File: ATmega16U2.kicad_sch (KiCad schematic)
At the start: 28 parts, among them J1 Conn_02x02_Odd_Even, J12 USB_B, J2 Conn_02x03_Top_Bottom, J3 Conn_PIC_ICSP_ICD, U3 ATmega16U2-A, Y2 Crystal

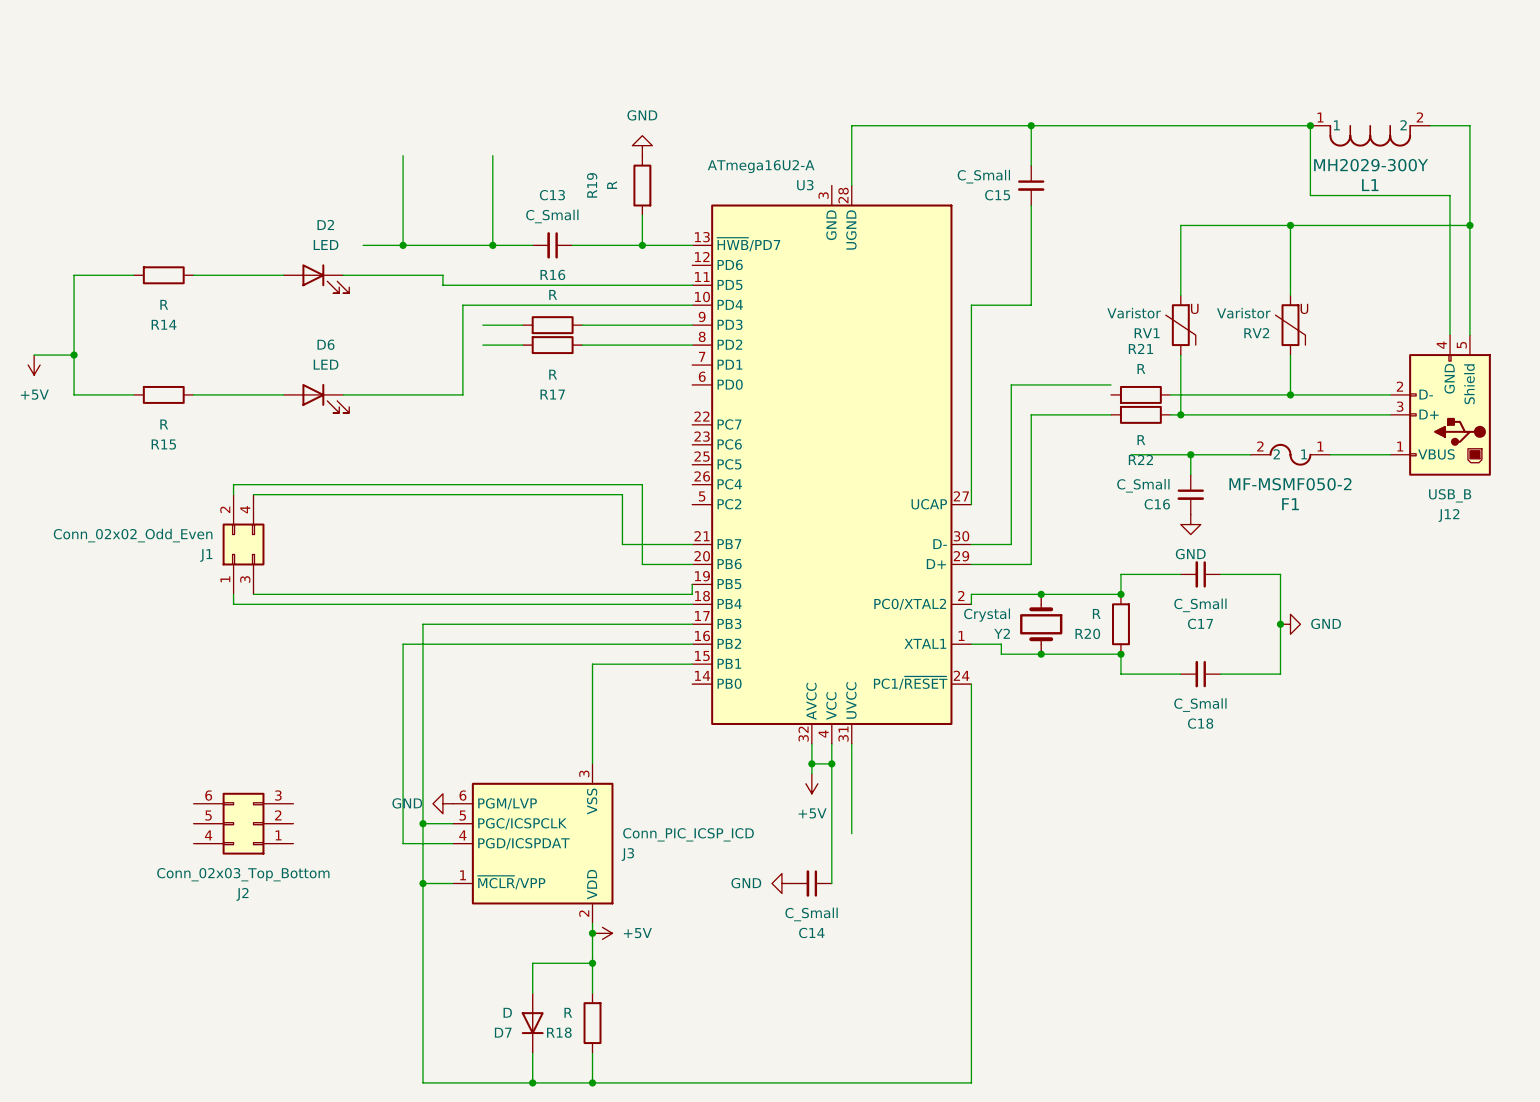
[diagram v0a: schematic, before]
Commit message: finished the schematic without mpower supply
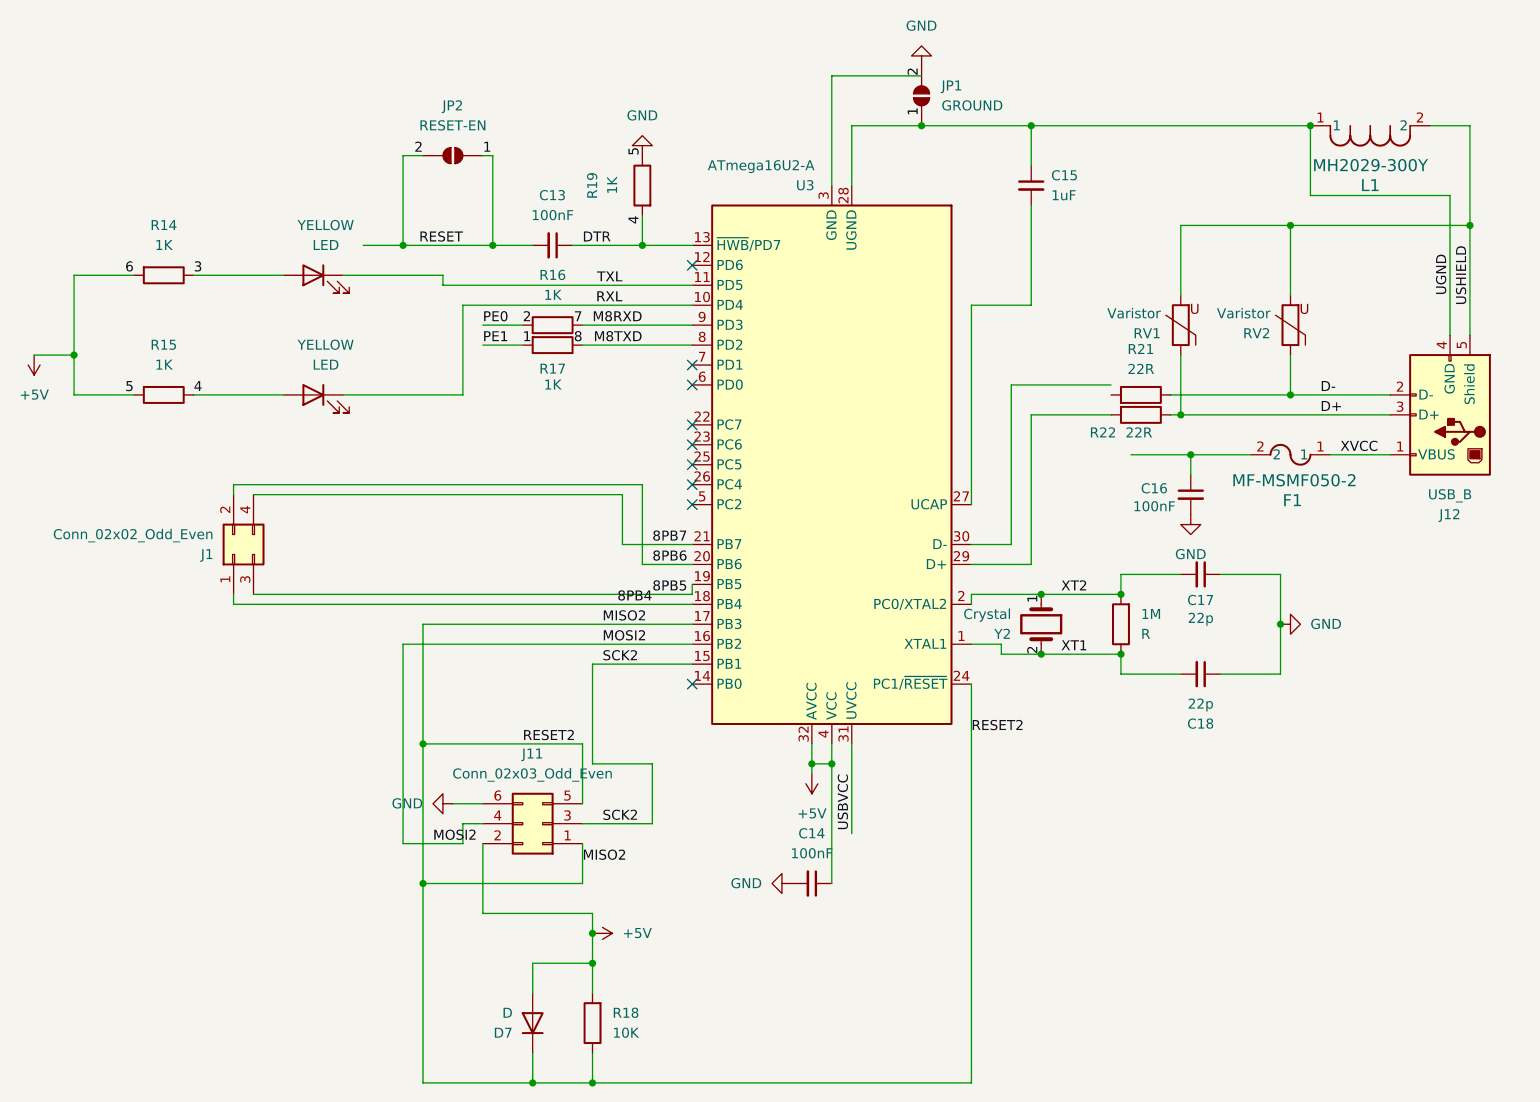
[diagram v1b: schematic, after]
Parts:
- removed J2: Conn_02x03_Top_Bottom, symbol Connector_Generic:Conn_02x03_Top_Bottom
- removed J3: Conn_PIC_ICSP_ICD, symbol Connector:Conn_PIC_ICSP_ICD
- added J11: Conn_02x03_Odd_Even, symbol Connector_Generic:Conn_02x03_Odd_Even
- added JP1: GROUND, symbol Jumper:SolderJumper_2_Open
- added JP2: RESET-EN, symbol Jumper:SolderJumper_2_Open
- C13, C14, C16: value C_Small -> 100nF
- C15: value C_Small -> 1uF
- C17, C18: value C_Small -> 22p
- R14, R15, R16, R17, R19: value R -> 1K
- R18: value R -> 10K
- R21, R22: value R -> 22R
- renumbered R20 to 1M, D2 to YELLOW, D6 to YELLOW
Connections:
- net GND is gone; now on net +5V: C14.2, C16.2, C17.1, C18.1, R19.1
- net +5V: now also J11.2 (Pin_2), J11.6 (Pin_6), JP1.2 (B)
- net D-: now reaches J12.2 (D-), R21.1, RV2.1
- net USHIELD: now reaches J12.5 (Shield), L1.2, RV1.2, RV2.2
- net 4: now reaches R15.1, YELLOW.2 (A)
- net 4: now also C13.1, R19.2, U3.13 (~{HWB}/PD7)
- net D+: now reaches J12.3 (D+), R22.1, RV1.1
- net 8PB4: now reaches J1.1 (Pin_1), U3.18 (PB4)
- net 8PB6: now reaches J1.2 (Pin_2), U3.20 (PB6)
- net 8PB5: now reaches J1.3 (Pin_3), U3.19 (PB5)
- net 8PB7: now reaches J1.4 (Pin_4), U3.21 (PB7)
- net TXL: now reaches U3.11 (PD5), YELLOW.1 (K)
- net 3: now reaches R14.1, YELLOW.2 (A)
- net MISO2: now reaches D7.1 (K), R18.1, U3.17 (PB3), U3.24 (PC1/~{RESET})
- net MISO2: now also J11.1 (Pin_1), J11.5 (Pin_5)
- net 1: now reaches 1M.1, C18.2, U3.1 (XTAL1), Y2.2
- net 1: now also 1M.2, C13.2, C17.2, R16.2, R17.2, U3.2 (PC0/XTAL2), U3.3 (GND), Y2.1, JP2.1 (A), JP2.2 (B)
- net UGND: now reaches C15.1, J12.4 (GND), L1.1, U3.28 (UGND)
- net UGND: now also JP1.1 (A)
- net RXL: now reaches U3.10 (PD4), YELLOW.1 (K)
- net 7: now reaches R16.1, U3.9 (PD3)
- net SCK2: now reaches U3.15 (PB1)
- net SCK2: now also J11.3 (Pin_3)
- net MOSI2: now reaches U3.16 (PB2)
- net MOSI2: now also J11.4 (Pin_4)
- net USBVCC: now reaches U3.31 (UVCC)
- net 8: now reaches R17.1, U3.8 (PD2)
- net XVCC: now reaches F1.1, J12.1 (VBUS)
- no-connect marks 0 -> 9

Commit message: my potential final schematic
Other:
- company: (none) -> GEVITON ENTERPRISES LIMITED
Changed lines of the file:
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@@
 		(title "ATmega16U2")
 		(date "2024-07-11")
+		(rev "0")
+		(company "GEVITON ENTERPRISES LIMITED")
 	)
 	(junction

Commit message: remaining with mh2029, the two connectors to finish footprint assignment
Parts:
- 1M1: renamed from 1M; footprint (none) -> Resistor_SMD:R_0201_0603Metric_Pad0.64x0.40mm_HandSolder
- C13, C14, C15, C16, C17, C18: footprint (none) -> Capacitor_SMD:C_0402_1005Metric_Pad0.74x0.62mm_HandSolder
- D7: footprint (none) -> Diode_SMD:D_0402_1005Metric_Pad0.77x0.64mm_HandSolder
- F1: footprint FUSE_F050-2 -> MF_MSMF050_2:FUSE_F050-2
- J11: footprint (none) -> Connector_PinHeader_1.00mm:PinHeader_2x03_P1.00mm_Vertical
- J12: footprint (none) -> Connector_USB:USB_B_OST_USB-B1HSxx_Horizontal
- JP1, JP2: footprint (none) -> Jumper:SolderJumper-2_P1.3mm_Open_RoundedPad1.0x1.5mm
- R14, R15, R16, R17, R18, R19, R21, R22: footprint (none) -> Resistor_SMD:R_0201_0603Metric_Pad0.64x0.40mm_HandSolder
- RV1, RV2: footprint (none) -> Varistor:Varistor_Panasonic_VF
- Y2: footprint (none) -> MCU-ATMEGA2560-16AU_TQFP100:TQFP100-0.5-14X14MM
- YELLOW1, YELLOW2: renamed from YELLOW; footprint (none) -> LED_SMD:LED_0201_0603Metric
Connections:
- net UGND is gone; now on net 1: C15.1, J12.4 (GND), JP1.1 (A), L1.1, U3.28 (UGND)
- net USBVCC: now also C16.1, F1.2
- net RD+: now reaches R22.2, U3.29 (D+)
- net RD-: now reaches U3.30 (D-)
- net RD-: now also R21.2
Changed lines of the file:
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@@
 	(wire
 		(pts
-			(xy 157.48 135.89) (xy 157.48 124.46)
-		)
-		(stroke
-			(width 0)
-			(type default)
-		)
-	)
-	(wire
-		(pts
 			(xy 137.16 73.66) (xy 123.19 73.66)
 		)
@@
 	(wire
 		(pts
+			(xy 157.48 124.46) (xy 157.48 132.08)
+		)
+		(stroke
+			(width 0)
+			(type default)
+		)
+	)
+	(wire
+		(pts
 			(xy 154.94 127) (xy 154.94 124.46)
 		)
@@
 	(wire
 		(pts
+			(xy 190.5 78.74) (xy 190.5 80.01)
+		)
+		(stroke
+			(width 0)
+			(type default)
+		)
+	)
+	(wire
+		(pts
 			(xy 124.46 114.3) (xy 124.46 127)
 		)
@@
 		)
 	)
+	(label "RD+"
+		(at 177.8 101.6 180)
+		(fields_autoplaced yes)
+		(effects
+			(font
+				(size 1.27 1.27)
+			)
+			(justify right bottom)
+		)
+	)
 	(label "MISO2"
 		(at 125.73 109.22 0)
@@
 	)
 	(label "1"
-		(at 166.37 44.45 90)
+		(at 165.1 45.72 90)
 		(fields_autoplaced yes)
 		(effects
@@
 		)
 	)
+	(label "RD-"
+		(at 177.8 99.06 180)
+		(fields_autoplaced yes)
+		(effects
+			(font
+				(size 1.27 1.27)
+			)
+			(justify right bottom)
+		)
+	)
 	(label "8PB7"
 		(at 132.08 99.06 0)
@@
 	)
 	(label "USBVCC"
-		(at 157.48 128.27 270)
+		(at 193.04 87.63 0)
+		(fields_autoplaced yes)
+		(effects
+			(font
+				(size 1.27 1.27)
+			)
+			(justify left bottom)
+		)
+	)
+	(label "USBVCC"
+		(at 157.48 132.08 270)
 		(fields_autoplaced yes)
 		(effects
@@
 			)
 		)
-		(property "Footprint" ""
+		(property "Footprint" "Varistor:Varistor_Panasonic_VF"
 			(at 215.138 71.12 90)
 			(effects
@@
 			)
 		)
-		(property "Footprint" ""
+		(property "Footprint" "Resistor_SMD:R_0201_0603Metric_Pad0.64x0.40mm_HandSolder"
 			(at 69.85 78.232 90)
 			(effects
@@
 			)
 		)
-		(property "Footprint" ""
+		(property "Footprint" "Resistor_SMD:R_0201_0603Metric_Pad0.64x0.40mm_HandSolder"
 			(at 194.31 80.772 90)
 			(effects
@@
 		(on_board yes)
 		(dnp no)
-		(property "Reference" "YELLOW"
+		(property "Reference" "YELLOW1"
 			(at 90.4875 58.42 0)
 			(effects
@@
 			)
 		)
-		(property "Footprint" ""
+		(property "Footprint" "LED_SMD:LED_0201_0603Metric"
 			(at 88.9 64.77 0)
 			(effects
@@
 			(project "arduino-mega-2560"
 				(path "/01593c05-32ee-43cc-9d3f-a6fed62a39f4/b6f834a9-11ca-4a09-9cf4-5366685f0c51"
-					(reference "YELLOW")
+					(reference "YELLOW1")
 					(unit 1)
 				)
@@
 			)
 		)
-		(property "Footprint" ""
+		(property "Footprint" "Resistor_SMD:R_0201_0603Metric_Pad0.64x0.40mm_HandSolder"
 			(at 126.238 160.02 90)
 			(effects
@@
 			)
 		)
-		(property "Footprint" ""
+		(property "Footprint" "Resistor_SMD:R_0201_0603Metric_Pad0.64x0.40mm_HandSolder"
 			(at 69.85 62.992 90)
 			(effects
@@
 			)
 		)
-		(property "Footprint" ""
+		(property "Footprint" "Resistor_SMD:R_0201_0603Metric_Pad0.64x0.40mm_HandSolder"
 			(at 132.588 53.34 90)
 			(effects
@@
 			)
 		)
-		(property "Footprint" ""
+		(property "Footprint" "Capacitor_SMD:C_0402_1005Metric_Pad0.74x0.62mm_HandSolder"
 			(at 201.93 115.57 0)
 			(effects
@@
 		(dnp no)
 		(fields_autoplaced yes)
-		(property "Reference" "1M"
+		(property "Reference" "1M1"
 			(at 194.31 107.9499 0)
 			(effects
@@
 			)
 		)
-		(property "Footprint" ""
+		(property "Footprint" "Resistor_SMD:R_0201_0603Metric_Pad0.64x0.40mm_HandSolder"
 			(at 193.548 109.22 90)
 			(effects
@@
 			(project "arduino-mega-2560"
 				(path "/01593c05-32ee-43cc-9d3f-a6fed62a39f4/b6f834a9-11ca-4a09-9cf4-5366685f0c51"
-					(reference "1M")
+					(reference "1M1")
 					(unit 1)
 				)
@@
 			)
 		)
-		(property "Footprint" ""
+		(property "Footprint" "Capacitor_SMD:C_0402_1005Metric_Pad0.74x0.62mm_HandSolder"
 			(at 180.34 53.34 0)
 			(effects
@@
 		(on_board yes)
 		(dnp no)
-		(property "Reference" "YELLOW"
+		(property "Reference" "YELLOW2"
 			(at 90.4875 73.66 0)
 			(effects
@@
 			)
 		)
-		(property "Footprint" ""
+		(property "Footprint" "LED_SMD:LED_0201_0603Metric"
 			(at 88.9 80.01 0)
 			(effects
@@
 			(project "arduino-mega-2560"
 				(path "/01593c05-32ee-43cc-9d3f-a6fed62a39f4/b6f834a9-11ca-4a09-9cf4-5366685f0c51"
-					(reference "YELLOW")
+					(reference "YELLOW2")
 					(unit 1)
 				)
@@
 			)
 		)
-		(property "Footprint" ""
+		(property "Footprint" "Resistor_SMD:R_0201_0603Metric_Pad0.64x0.40mm_HandSolder"
 			(at 119.38 72.898 90)
 			(effects
@@
 			)
 		)
-		(property "Footprint" ""
+		(property "Footprint" "Diode_SMD:D_0402_1005Metric_Pad0.77x0.64mm_HandSolder"
 			(at 116.84 160.02 0)
 			(effects
@@
 			)
 		)
-		(property "Footprint" ""
+		(property "Footprint" "Jumper:SolderJumper-2_P1.3mm_Open_RoundedPad1.0x1.5mm"
 			(at 166.37 41.91 0)
 			(effects
@@
 			)
 		)
-		(property "Footprint" ""
+		(property "Footprint" "Capacitor_SMD:C_0402_1005Metric_Pad0.74x0.62mm_HandSolder"
 			(at 152.4 142.24 0)
 			(effects
@@
 			)
 		)
-		(property "Footprint" ""
+		(property "Footprint" "Capacitor_SMD:C_0402_1005Metric_Pad0.74x0.62mm_HandSolder"
 			(at 119.38 60.96 0)
 			(effects
@@
 			)
 		)
-		(property "Footprint" ""
+		(property "Footprint" "Capacitor_SMD:C_0402_1005Metric_Pad0.74x0.62mm_HandSolder"
 			(at 200.66 92.71 0)
 			(effects
@@
 			)
 		)
-		(property "Footprint" ""
+		(property "Footprint" "Jumper:SolderJumper-2_P1.3mm_Open_RoundedPad1.0x1.5mm"
 			(at 106.68 49.53 0)
 			(effects
@@
 			)
 		)
-		(property "Footprint" ""
+		(property "Footprint" "Capacitor_SMD:C_0402_1005Metric_Pad0.74x0.62mm_HandSolder"
 			(at 201.93 102.87 0)
 			(effects
@@
 			)
 		)
-		(property "Footprint" ""
+		(property "Footprint" "Varistor:Varistor_Panasonic_VF"
 			(at 201.168 71.12 90)
 			(effects
@@
 			)
 		)
-		(property "Footprint" ""
+		(property "Footprint" "Resistor_SMD:R_0201_0603Metric_Pad0.64x0.40mm_HandSolder"
 			(at 194.31 81.788 90)
 			(effects
@@
 			)
 		)
-		(property "Footprint" ""
+		(property "Footprint" "MCU-ATMEGA2560-16AU_TQFP100:TQFP100-0.5-14X14MM"
 			(at 181.61 109.22 0)
 			(effects
@@
 			)
 		)
-		(property "Footprint" ""
+		(property "Footprint" "Resistor_SMD:R_0201_0603Metric_Pad0.64x0.40mm_HandSolder"
 			(at 119.38 71.882 90)
 			(effects
@@
 			)
 		)
-		(property "Footprint" ""
+		(property "Footprint" "Connector_PinHeader_1.00mm:PinHeader_2x03_P1.00mm_Vertical"
 			(at 118.11 134.62 0)
 			(effects
@@
 			)
 		)
-		(property "Footprint" "FUSE_F050-2"
+		(property "Footprint" "MF_MSMF050_2:FUSE_F050-2"
 			(at 218.44 87.63 0)
 			(effects
@@
 			)
 		)
-		(property "Footprint" ""
+		(property "Footprint" "Connector_USB:USB_B_OST_USB-B1HSxx_Horizontal"
 			(at 229.87 81.28 0)
 			(effects
